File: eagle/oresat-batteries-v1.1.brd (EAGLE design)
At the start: 98.6 x 95.3 mm, 103 parts, among them IC1 74AHC1G08DBV, J1 2MM-RA-1X8, Q1 CSD16340Q3, Q2 CSD16340Q3, Q3 TPN4R712MD, Q4 TPN4R712MD, Q5 TPN4R712MD, Q6 TPN4R712MD, Q7 CSD16340Q3, U1 LM3761, U10 LTC4412, U11 MAX17055, U12 LTC4412, U13 LTC4412, U14 STM32F042K6, U15 TCAN330, U2 MC74HC1G04DFT1GOSCT, U3 BQ2970, U4 LTC4411, U5 LTC4411, U6 LTC4411, U7 LTC4411, U8 MC74HC1G04DFT1GOSCT, U9 LTC4412, X1 16MHz

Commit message: Updates after design review with Austin. Still some TODOs before layout.
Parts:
- removed TP24, TP25, TP26, TP27, TP28, TP29, TP31, TP32, TP33, TP34, TP35: TP, oresat-batteries:2MM_TP
- added R21: 10k, rcl:R0603
- added TP10: TP, oresat-batteries:2MM_TP
- moved TP23 212.7 mm to (-77.6, -436.4)
- moved TP21 174.3 mm to (-77.6, -416.4)
- moved TP19 152.0 mm to (-77.6, -396.4)
- moved TP22 136.6 mm to (-77.6, -376.4)
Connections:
- new net N$10: TP21.P$1, U14.13
- new net N$9: C4.1, R1.1, TP5.P$1, U3.5
- net 3.3V: no longer Q7.P$5, Q7.P$6, Q7.P$7, Q7.P$8, Q7.P$9, TP22.P$1, TP29.P$1
- net 5V: now also Q7.P$5, Q7.P$6, Q7.P$7, Q7.P$8, Q7.P$9, R21.2; no longer C8.1, U11.10
- net BATT-: now also IC1.3
- net CANH: no longer TP31.P$1, TP34.P$1
- net CANL: no longer TP32.P$1, TP33.P$1
- net CAN_LSTN: now also TP19.P$1
- net CAN_RX: now also TP10.P$1
- net CAN_TX: now also TP22.P$1
- net GND: no longer IC1.3
- net HEAT: now also R21.1
- net N$4: now also TP23.P$1
- net NRESET: no longer TP28.P$1
- net STM_DEBUG: no longer TP23.P$1
- net SWCLK: no longer TP27.P$1
- net SWDIO: no longer TP26.P$1
- net SYSSHD: no longer C4.1, R1.1, TP5.P$1, U3.5
- net USART2_RX: no longer TP19.P$1, TP24.P$1
- net USART2_TX: no longer TP21.P$1, TP25.P$1
- net VBATT: now also C8.1, U11.10
- net VSOLAR: no longer TP35.P$1

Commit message: Preliminary layout.
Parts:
- removed J1: 2MM-RA-1X8, oresat-batteries:CF-2MM-RA-1X8-PRECIDIP-831
- removed TP6: TP, oresat-batteries:2MM_TP
- added J2: CORTEX_DEBUG_PTH, SparkFun-Connectors:2X5-PTH-1.27MM
- added TP24: TP, oresat-batteries:2MM_TP
- added U$1, U$2: MF-SMDF050, fuse:MF-SMDF050
- moved TP23 543.9 mm to (87.3, 81.8)
- moved TP21 515.6 mm to (78.3, 75.0)
- moved TP19 491.2 mm to (56.5, 76.2)
- moved TP22 490.2 mm to (85.2, 86.0)
- moved TP10 473.4 mm to (87.7, 87.2)
- moved R21 440.2 mm to (57.0, 72.3), turned to 270 degrees
- moved D1 401.9 mm to (41.9, 62.5), turned to 270 degrees
- moved D3 396.0 mm to (45.5, 59.5)
- moved D2 395.2 mm to (37.2, 66.0), turned to 270 degrees
- moved TP20 389.3 mm to (28.2, 43.2)
- moved JP1 366.9 mm to (28.4, 79.2), turned to 180 degrees
- moved TP11 346.7 mm to (44.6, 64.0)
- moved TP12 335.8 mm to (10.0, 59.0)
- moved TP14 335.3 mm to (39.5, 58.4)
- moved R8 312.2 mm to (54.9, 72.5), turned to 270 degrees
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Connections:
- net COUT renamed BQCOUT
- net N$10 renamed TP21
- net N$3 renamed TEMPSENSE
- net N$5 renamed BGDOUT
- net N$9 renamed BQBAT
- removed net 5V: Q7.P$5, Q7.P$6, Q7.P$7, Q7.P$8, Q7.P$9, R21.2
- removed net N$6: D1.1, JP1.8
- removed net STM_DEBUG: J1.8, U14.6
- removed net VBATT: B1.POS, C1.1, C2.1, C7.1, C8.1, IC1.5, Q3.5, Q3.6, Q3.7, Q3.8, Q4.5, Q4.6, Q4.7, Q4.8, R1.2, R2.2, R4.2, R6.1, R8.2, TP12.P$1, U1.1, U10.1, U11.10, U2.3, U6.5, U7.5, U8.3, U9.1
- new net INFUSE: U$1.1, U4.1, U5.1
- new net N$14: TP24.P$1, U14.6
- new net OUTFUSE: Q5.1, Q5.2, Q5.3, Q6.1, Q6.2, Q6.3, U$2.1, U12.6, U13.6
- new net V_BATT: B1.POS, C1.1, C2.1, C7.1, C8.1, IC1.5, Q3.5, Q3.6, Q3.7, Q3.8, Q4.5, Q4.6, Q4.7, Q4.8, Q7.P$5, Q7.P$6, Q7.P$7, Q7.P$8, Q7.P$9, R1.2, R2.2, R21.2, R4.2, R6.1, R8.2, TP12.P$1, U1.1, U10.1, U11.10, U2.3, U6.5, U7.5, U8.3, U9.1
- net !SHUTDOWN: now also D1.1, JP1.8
- net 3.3V: now also J2.1; no longer J1.2
- net GND: now also J2.3, J2.5, J2.7, J2.9; no longer J1.1
- net N$16: no longer U13.6
- net NRESET: now also J2.10; no longer J1.3
- net SWCLK: now also J2.4; no longer J1.4
- net SWDIO: now also J2.2; no longer J1.5
- net USART2_RX: no longer J1.7
- net USART2_TX: no longer J1.6
- net VSOLAR: now also U$1.2, U$2.2; no longer Q5.1, Q5.2, Q5.3, Q6.1, Q6.2, Q6.3, TP6.P$1, U12.6, U4.1, U5.1
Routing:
- net NRESET: track 0.00 -> 106.9 mm, vias 0 -> 4
- net USART2_RX: track 0.00 -> 99.9 mm, vias 0 -> 1
- net U7STAT: track 0.00 -> 99.3 mm, vias 0 -> 7
- net SWCLK: track 0.00 -> 95.3 mm, vias 0 -> 2
- net USART2_TX: track 0.00 -> 94.7 mm, vias 0 -> 1
- net SWDIO: track 0.00 -> 94.4 mm, vias 0 -> 2
- net U9STAT: track 0.00 -> 90.1 mm, vias 0 -> 3
- net ALERT: track 0.00 -> 86.0 mm, vias 0 -> 5
- net SCL: track 0.00 -> 72.7 mm, vias 0 -> 5
- net SDA: track 0.00 -> 71.3 mm, vias 0 -> 4
- net HEAT: track 0.00 -> 62.6 mm, vias 0 -> 2
- net TO_DCHG: track 0.00 -> 55.0 mm, vias 0 -> 6
- net TO_CHG: track 0.00 -> 49.3 mm, vias 0 -> 3
- net DSCHG_SHD: track 0.00 -> 46.6 mm
- net CAN_RX: track 0.00 -> 39.1 mm, vias 0 -> 1
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- added copper zone on layer 1, net !SHUTDOWN
- added copper zone on layer 16, net !SHUTDOWN
- added copper zone on layer 1, net 3.3V
- added copper zone on layer 4, net 3.3V
- added copper zone on layer 1, net 4411MB
- added copper zone on layer 1, net 4411_MT
- added copper zone on layer 1, net BATT-
- added copper zone on layer 16, net BATT-
- added copper zone on layer 4, net BATT-
- added copper zone on layer 1, net BETSHUT
- added copper zone on layer 1, net BQBAT
- added copper zone on layer 1, net CANH
- added copper zone on layer 16, net CANH
- added copper zone on layer 1, net CANL
- added copper zone on layer 16, net CANL
- added copper zone on layer 1, net CHG_CTL
- added copper zone on layer 16, net CHG_CTL
- added copper zone on layer 1, net CHG_SHD
- added copper zone on layer 1, net C_SENSE
- added copper zone on layer 5, net C_SENSE
- added copper zone on layer 1, net DCHG_CTL
- added copper zone on layer 16, net DCHG_CTL
- added copper zone on layer 1, net GND
- added copper zone on layer 1, net INFUSE
- added copper zone on layer 1, net N$1
- added copper zone on layer 1, net N$11
- added copper zone on layer 16, net N$13
- added copper zone on layer 1, net N$18
- added copper zone on layer 1, net OUTFUSE
- added copper zone on layer 1, net SYSSHD
- added copper zone on layer 1, net TO_CHG
- added copper zone on layer 1, net USART2_RX
- added copper zone on layer 1, net USART2_TX
- added copper zone on layer 1, net VSOLAR
- added copper zone on layer 16, net VSOLAR
- added copper zone on layer 1, net V_BATT
- added copper zone on layer 16, net V_BATT
- added copper zone on layer 4, net V_BATT

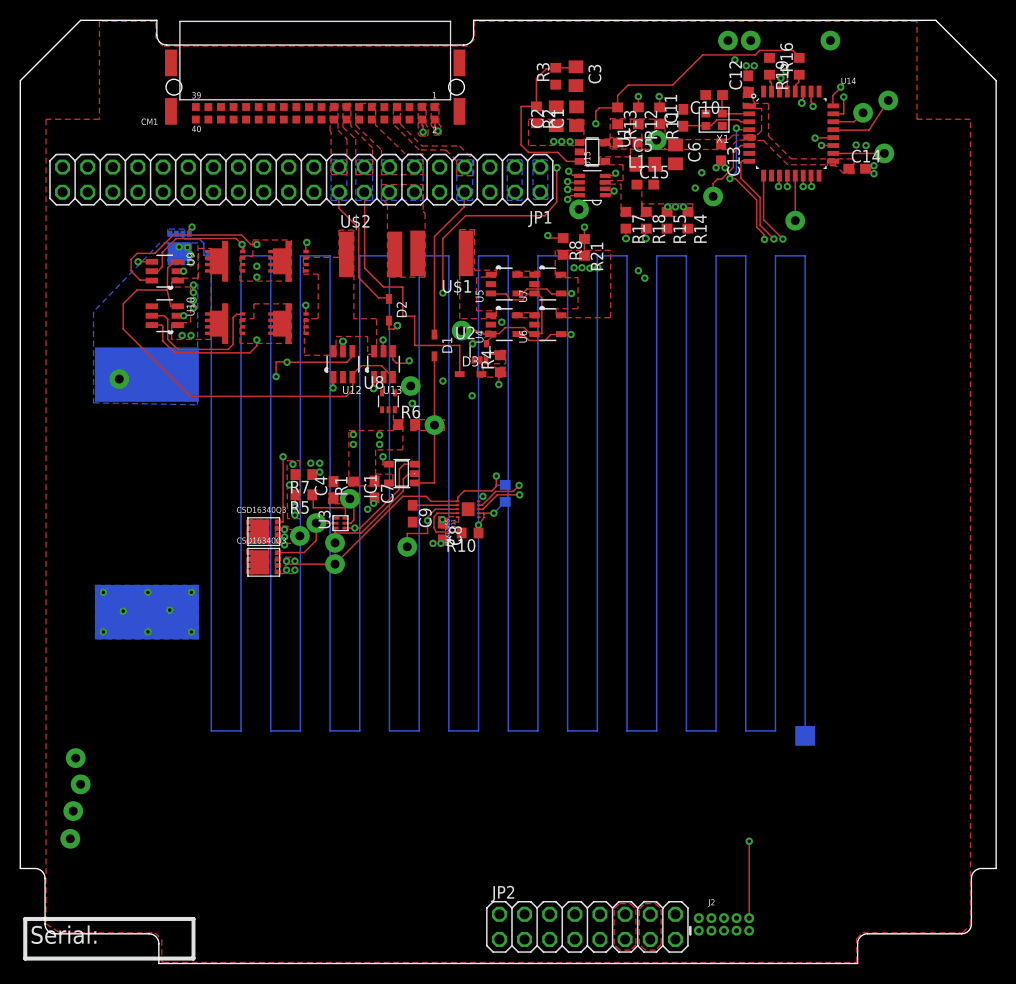
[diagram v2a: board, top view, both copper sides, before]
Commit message: Cosmetics and polygons.
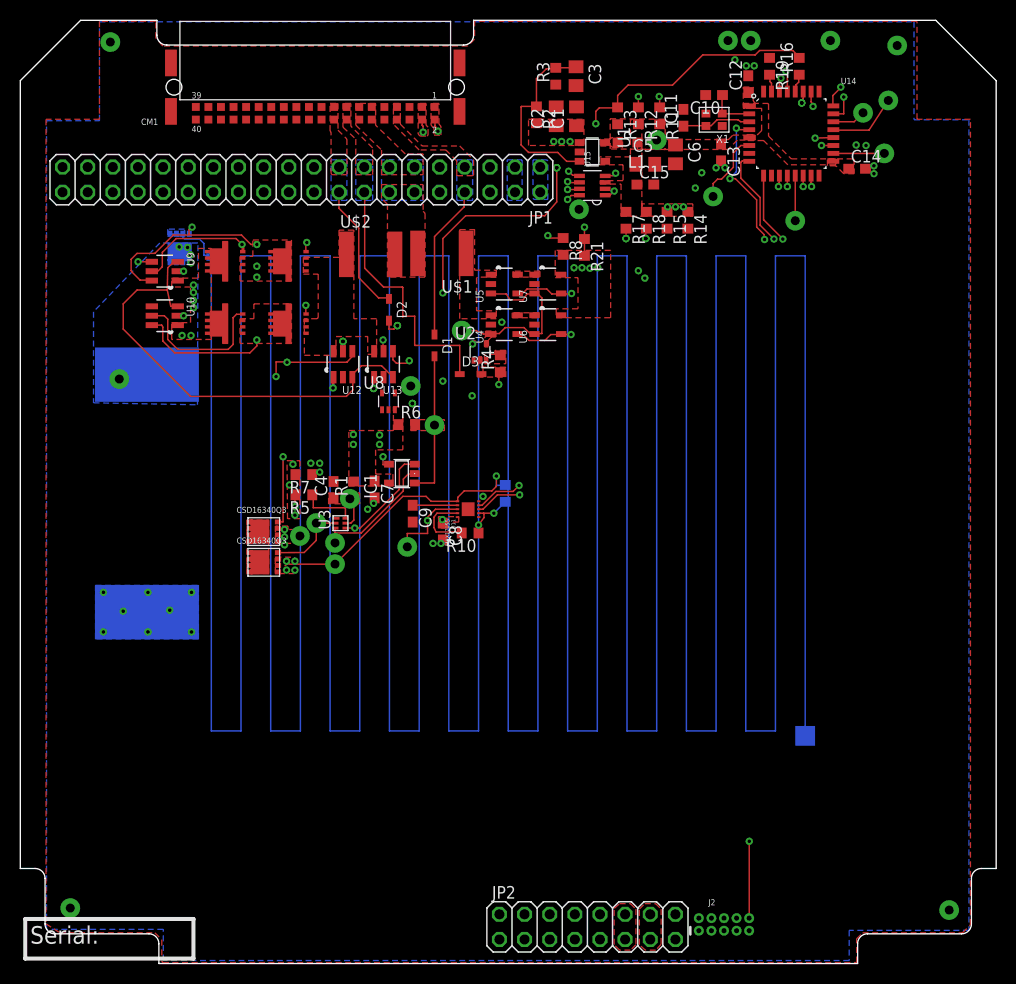
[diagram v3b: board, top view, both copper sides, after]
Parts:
- moved TP1 109.9 mm to (88.6, 92.8)
- moved TP4 89.1 mm to (93.8, 5.40)
- moved TP2 75.1 mm to (9.10, 93.1)
- moved TP3 7.00 mm to (5.05, 5.60)
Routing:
- added copper zone on layer 16, net GND
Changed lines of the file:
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@@
 <setting verticaltext="up"/>
 </settings>
-<grid distance="0.05" unitdist="mm" unit="mm" style="lines" multiple="1" display="yes" altdistance="0.025" altunitdist="inch" altunit="inch"/>
+<grid distance="0.5" unitdist="mm" unit="mm" style="lines" multiple="1" display="yes" altdistance="0.025" altunitdist="inch" altunit="inch"/>
 <layers>
 <layer number="1" name="Top" color="4" fill="1" visible="yes" active="yes"/>
@@
 <element name="Q2" library="oresat-batteries" package="Q3" value="CSD16340Q3" x="24.6" y="40.5375" rot="R90"/>
 <element name="Q1" library="oresat-batteries" package="Q3" value="CSD16340Q3" x="24.6" y="43.6375" rot="R90"/>
-<element name="TP3" library="oresat-batteries" package="2MM_TP" value="TP" x="5.05" y="12.6"/>
-<element name="TP4" library="oresat-batteries" package="2MM_TP" value="TP" x="5.35" y="15.4"/>
+<element name="TP3" library="oresat-batteries" package="2MM_TP" value="TP" x="5.05" y="5.6"/>
+<element name="TP4" library="oresat-batteries" package="2MM_TP" value="TP" x="93.85" y="5.4"/>
 <element name="JP2" library="pinhead" library_urn="urn:adsk.eagle:library:325" package="2X08" package3d_urn="urn:adsk.eagle:package:22481/2" value="" x="57.3" y="3.7" smashed="yes" rot="R180">
 <attribute name="NAME" x="50.06" y="7.825" size="1.27" layer="25" ratio="10" rot="R180"/>
@@
 <element name="B1" library="oresat-batteries" package="2AH_605060" value="2AHBATT" x="49.3" y="47.5" rot="MR90"/>
 <element name="R20" library="oresat-batteries" package="RES_HEATER" value="4.19" x="49.3" y="47.5" rot="MR270"/>
-<element name="TP1" library="oresat-batteries" package="2MM_TP" value="TP" x="5.6" y="20.75"/>
-<element name="TP2" library="oresat-batteries" package="2MM_TP" value="TP" x="6.1" y="18.1"/>
+<element name="TP1" library="oresat-batteries" package="2MM_TP" value="TP" x="88.6" y="92.75"/>
+<element name="TP2" library="oresat-batteries" package="2MM_TP" value="TP" x="9.1" y="93.1"/>
 <element name="TP18" library="oresat-batteries" package="2MM_TP" value="TP" x="81.85" y="93.25"/>
 <element name="TP7" library="oresat-batteries" package="2MM_TP" value="TP" x="41.85" y="54.4"/>
@@
 <via x="30.25" y="50.55" extent="1-16" drill="0.35"/>
 <via x="30.25" y="49.65" extent="1-16" drill="0.35"/>
-<wire x1="73.64" y1="3.315" x2="79.3" y2="23" width="0" layer="19" extent="16-16"/>
+<polygon width="0.1524" layer="16" thermals="no">
+<vertex x="8" y="95.15"/>
+<vertex x="90.3" y="95.15"/>
+<vertex x="90.3" y="85.25"/>
+<vertex x="95.85" y="85.25"/>
+<vertex x="95.85" y="3.35"/>
+<vertex x="83.75" y="3.35"/>
+<vertex x="83.75" y="0.3"/>
+<vertex x="14.45" y="0.3"/>
+<vertex x="14.45" y="3.45"/>
+<vertex x="2.65" y="3.45"/>
+<vertex x="2.65" y="85.15"/>
+<vertex x="8" y="85.15"/>
+</polygon>
 <wire x1="47.55" y1="64.55" x2="45.8" y2="62.65" width="0" layer="19" extent="1-1"/>
 <wire x1="35.7" y1="46.5" x2="39.65" y2="44.6" width="0" layer="19" extent="1-1"/>
-<wire x1="16.5" y1="69.95" x2="16.5" y2="65.45" width="0" layer="19" extent="1-1"/>
 <wire x1="46.325" y1="46.7" x2="42.7" y2="42.8" width="0" layer="19" extent="1-1"/>
 </signal>

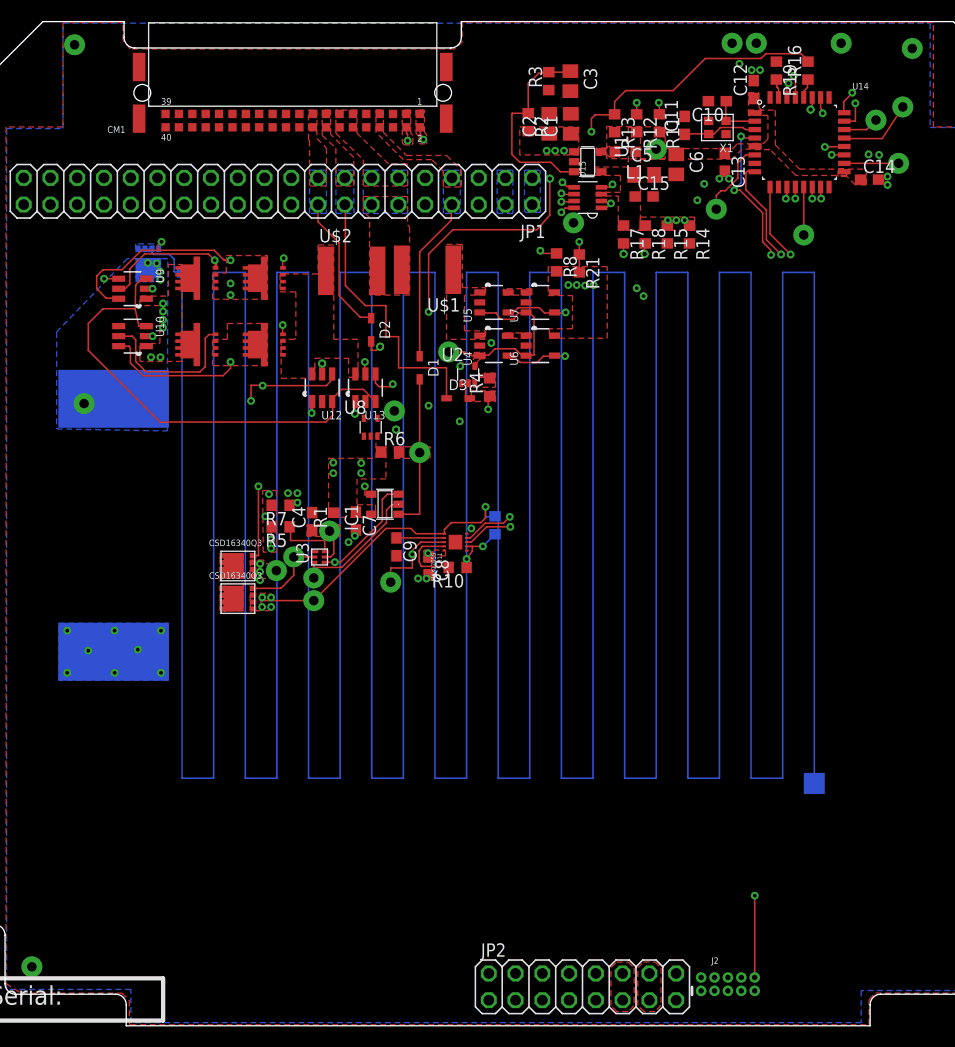
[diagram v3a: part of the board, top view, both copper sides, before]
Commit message: Moved to OSH Park 4 layer DRU, fixed some bad/useless layers.
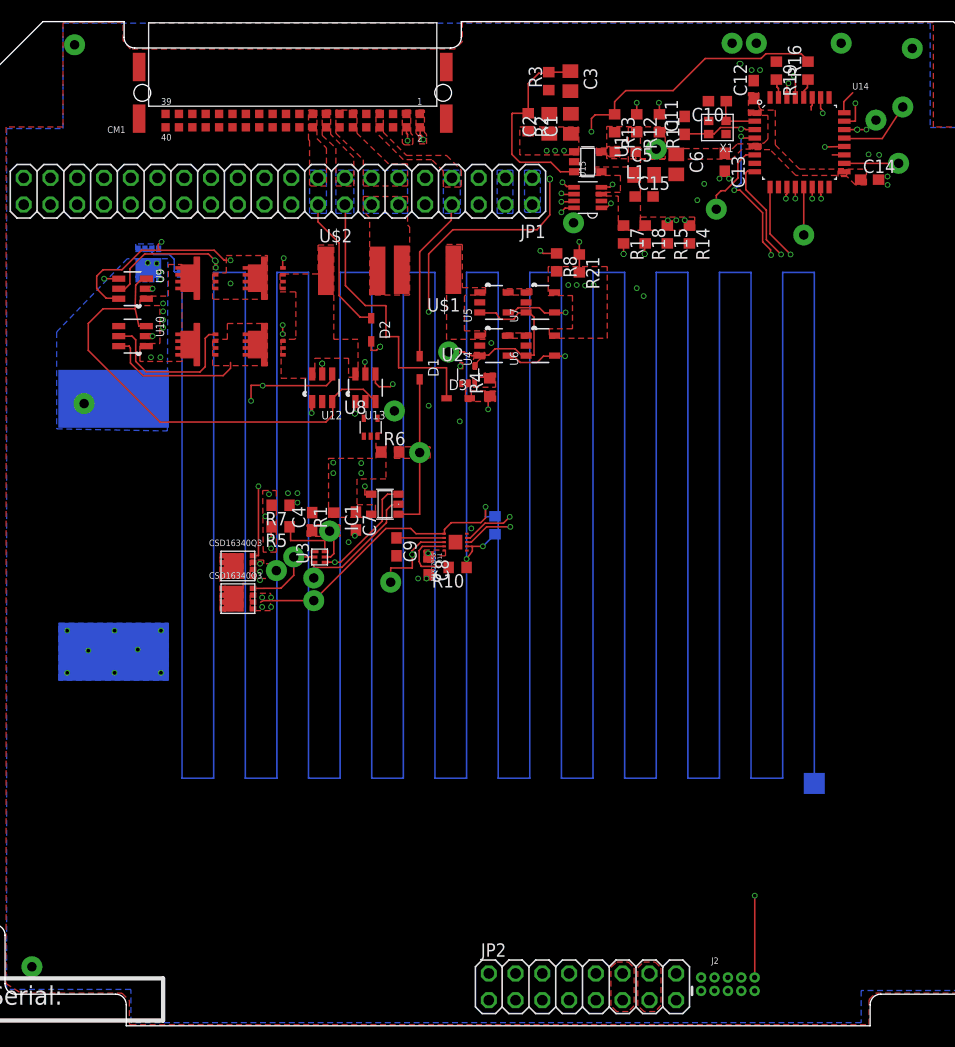
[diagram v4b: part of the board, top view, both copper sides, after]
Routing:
- net NRESET: track 106.9 -> 106.1 mm, vias 4 -> 5
- net U7STAT: vias 7 -> 5
- net TO_DCHG: vias 6 -> 4
- net SWCLK: vias 2 -> 1
- net SCL: vias 5 -> 6
- net N$18: vias 3 -> 2
- net N$16: vias 2 -> 3
- net N$12: vias 1 -> 3
- net N$11: vias 4 -> 3
- net CAN_TX: vias 1 -> 4
- net CAN_LSTN: vias 2 -> 1
- net ALERT: vias 5 -> 8
- added copper zone on layer 2, net 3.3V
- added copper zone on layer 2, net BATT-
- added copper zone on layer 15, net C_SENSE
- added copper zone on layer 2, net V_BATT
- removed copper zone on layer 4, net 3.3V
- removed copper zone on layer 4, net BATT-
- removed copper zone on layer 5, net C_SENSE
- removed copper zone on layer 4, net V_BATT
